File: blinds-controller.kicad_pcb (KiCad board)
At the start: 2 copper layers, 50.8 x 69.9 mm, 15 parts, among them J1 Jack-DC, J2 Conn_01x05_Female, U1 MP1584EN-LF-Z, U2 ESP32-S2-WROOM, U3 ULN2003A

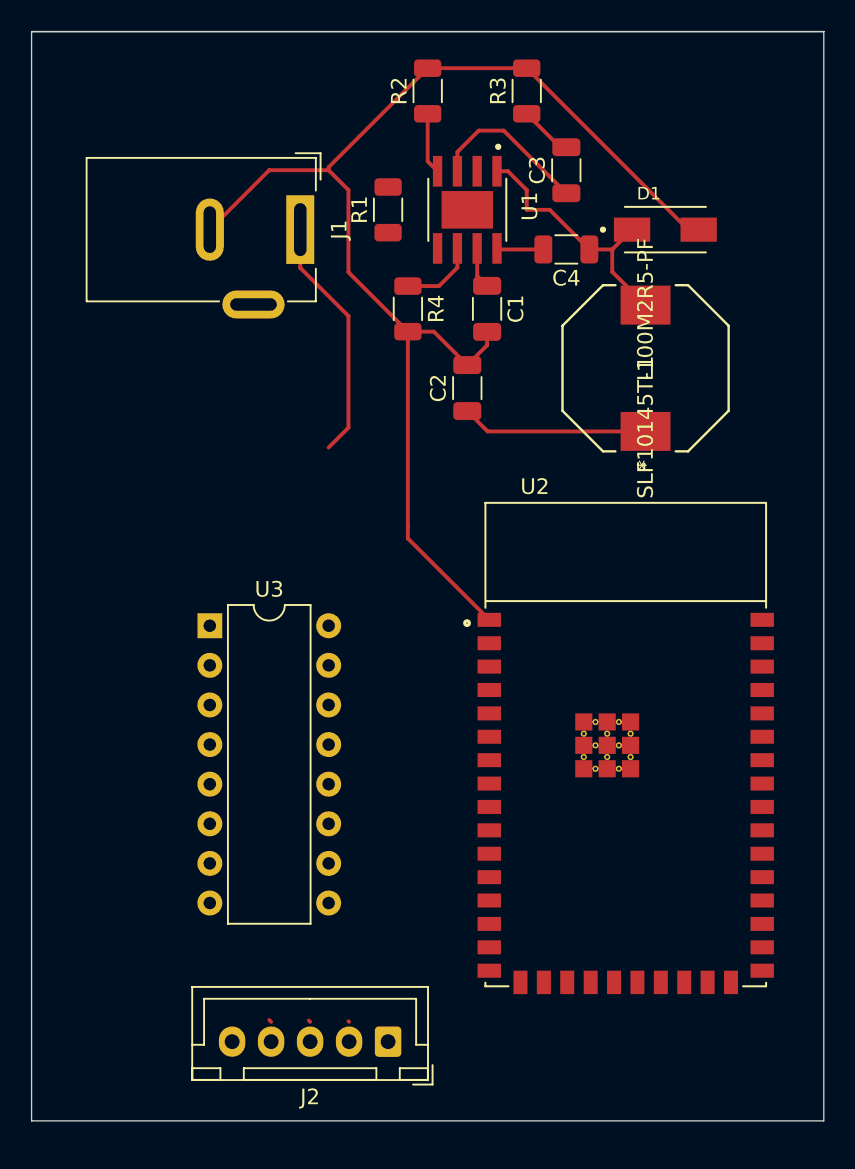
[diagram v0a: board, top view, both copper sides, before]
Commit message: First routed version of PCB
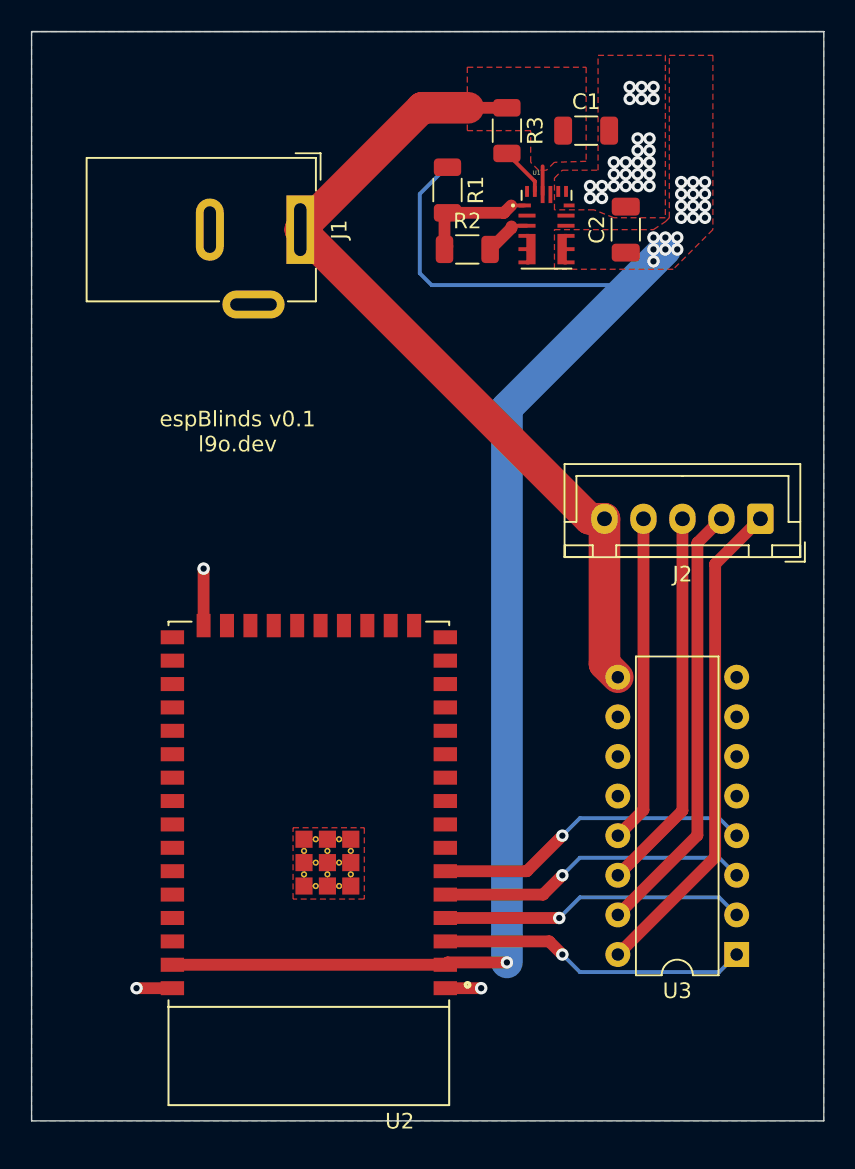
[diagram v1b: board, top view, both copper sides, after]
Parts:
- removed C3: 220pF, Capacitor_SMD:C_1206_3216Metric
- removed C4: 100nF, Capacitor_SMD:C_1206_3216Metric
- removed D1: B340A-13-F, B340A-13-F:DIOM5226X240N
- removed L1: SLF10145T-100M2R5-PF, SLF10145T-100:SLF10145T-100M2R5-PF
- removed R4: 200k, Resistor_SMD:R_1206_3216Metric
- C1: value 10uF -> 10uf
- R1: value 124k -> 75k
- R2: value 40.2k -> 24k
- R3: value 68.1k -> 100k
- U1: value MP1584EN-LF-Z -> MPM3610AGQV-P; footprint MP1584EN-LF-Z:SOIC127P600X170-9N -> footprints:CONV_MPM3620AGQV-P
- moved J2 41.2 mm to (100.1, 50.3)
- moved U3 39.8 mm to (98.6, 78.2), turned to 180 degrees
- moved U2 21.7 mm to (71.1, 72.4), turned to 180 degrees
- moved C2 14.4 mm to (91.4, 31.8)
- moved C1 13.1 mm to (88.9, 25.4), turned to 0 degrees
- moved R2 10.5 mm to (81.3, 33.0), turned to 0 degrees
- moved U1 5.24 mm to (86.4, 31.8), turned to 0 degrees
- moved R1 4.02 mm to (80.0, 29.2), turned to 270 degrees
- moved R3 2.84 mm to (83.8, 25.4), turned to 270 degrees
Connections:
- R3 pad 1: Net-(C3-Pad2) -> +12V
- R3 pad 2: GND -> Net-(R3-Pad2)
- U1 pad 1: Net-(C4-Pad1) -> Net-(R1-Pad2)
- U1 pad 3: Net-(C3-Pad1) -> GND
- U1 pad 4: Net-(R1-Pad2) -> Net-(U1-Pad19)
- U1 pad 5: GND -> Net-(U1-Pad19)
- U1 pad 6: Net-(R4-Pad1) -> Net-(U1-Pad19)
- U1 pad 7: +12V -> +3V3
- U1 pad 8: Net-(C4-Pad2) -> +3V3
- U1 pad 9: (no net) -> +3V3
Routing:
- net +3V3: track 12.0 -> 95.4 mm, vias 0 -> 20
- net GND: track 80.5 -> 11.3 mm, vias 0 -> 29
- net +12V: track 18.6 -> 56.0 mm
- net Net-(J2-Pad1): track 0.00 -> 31.7 mm
- net Net-(J2-Pad2): track 0.06 -> 28.2 mm
- net Net-(J2-Pad3): track 0.00 -> 24.6 mm
- net Net-(J2-Pad4): track 0.17 -> 21.0 mm
- net Stepper.D: track 0.00 -> 20.6 mm, vias 0 -> 1
- net Stepper.C: track 0.00 -> 20.1 mm, vias 0 -> 1
- net Stepper.A: track 0.00 -> 20.0 mm, vias 0 -> 1
- net Stepper.B: track 0.00 -> 19.7 mm, vias 0 -> 1
- net Net-(C4-Pad1): track 16.5 -> 0.00 mm
- net Net-(C3-Pad1): track 10.5 -> 0.00 mm
- net Net-(R4-Pad1): track 4.90 -> 0.00 mm
- net Net-(R1-Pad2): track 3.95 -> 8.23 mm
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- added copper zone on F.Cu, net +12V
- added copper zone on F.Cu, net +3V3
- added copper zone on B.Cu, net GND
- added copper zone on F.Cu, net GND
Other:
- board text added: "espBlinds v0.1 l9o.dev"

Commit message: Added headers for testing voltage
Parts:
- added J3: DC Check, Connector_PinHeader_2.54mm:PinHeader_1x03_P2.54mm_Vertical, F.Cu at (75.2, 42.7)
- J2: value Conn_01x05_Female -> Stepper Motor
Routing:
- net +3V3: track 95.4 -> 104.1 mm
- net +12V: track 56.0 -> 60.5 mm
- net GND: vias 29 -> 30

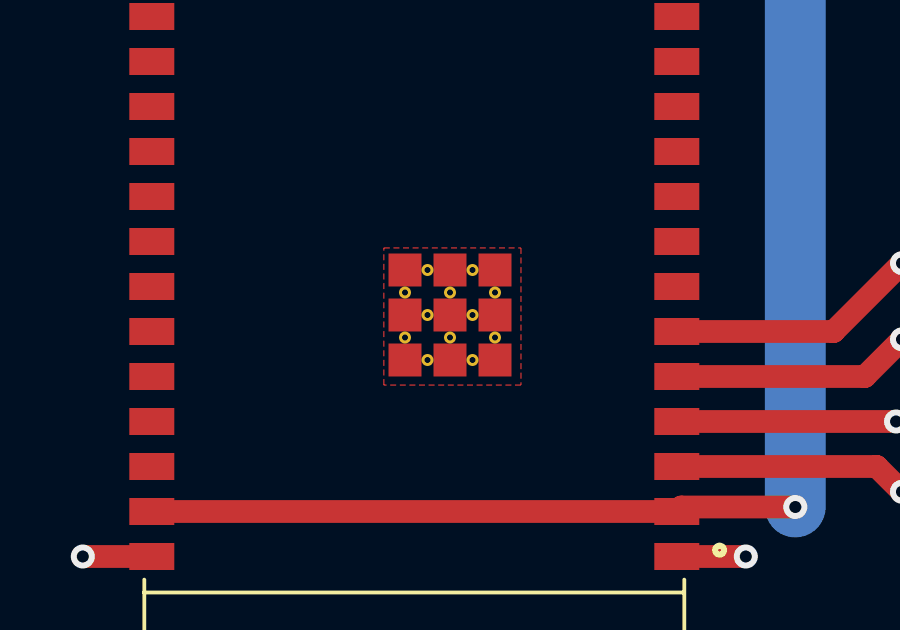
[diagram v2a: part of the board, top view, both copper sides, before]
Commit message: Added traces between GND pins on ESP32 bottom
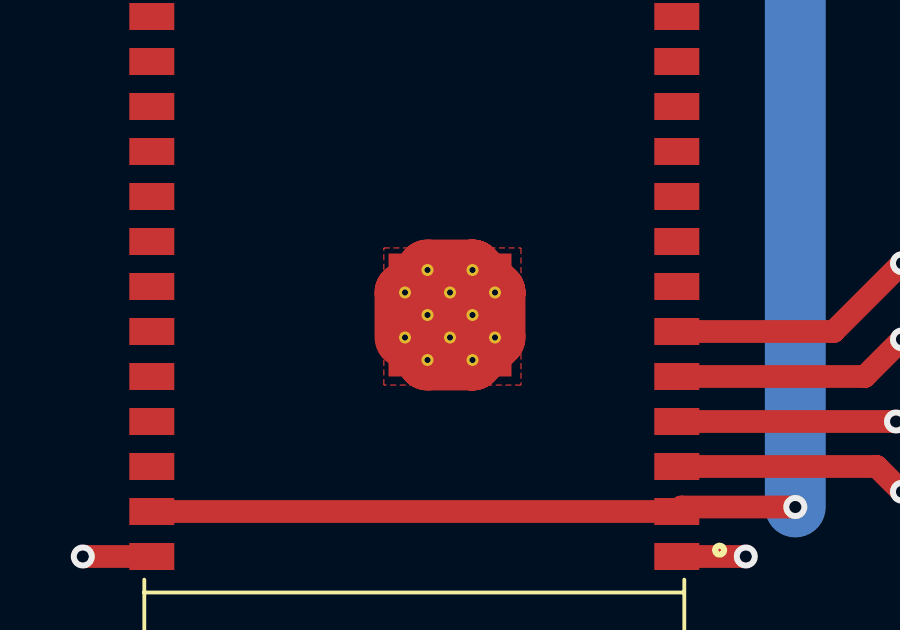
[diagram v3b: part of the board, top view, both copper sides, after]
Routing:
- net GND: track 11.3 -> 30.1 mm
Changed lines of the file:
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@@
     (thickness 1.6)
     (drawings 6)
-    (tracks 131)
+    (tracks 147)
     (zones 0)
     (modules 11)
@@
   (segment (start 83.78925 31.97325) (end 84.11383 31.64867) (width 0.76) (layer F.Cu) (net 2))
   (via (at 83.78925 31.97325) (size 0.8) (drill 0.4) (layers F.Cu B.Cu) (net 2))
+  (segment (start 73.06 70.84) (end 71.56 70.84) (width 2.03) (layer F.Cu) (net 2))
+  (segment (start 70.81 71.59) (end 70.81 73.09) (width 2.03) (layer F.Cu) (net 2))
+  (segment (start 71.56 73.84) (end 73.06 73.84) (width 2.03) (layer F.Cu) (net 2))
+  (segment (start 73.06 73.84) (end 73.81 73.09) (width 2.03) (layer F.Cu) (net 2))
+  (segment (start 73.81 73.09) (end 73.81 71.59) (width 2.03) (layer F.Cu) (net 2))
+  (segment (start 73.81 71.59) (end 73.06 70.84) (width 2.03) (layer F.Cu) (net 2))
+  (segment (start 72.31 73.09) (end 71.56 72.34) (width 2.03) (layer F.Cu) (net 2))
+  (segment (start 71.56 72.34) (end 72.31 71.59) (width 2.03) (layer F.Cu) (net 2))
+  (segment (start 72.31 71.59) (end 73.06 72.34) (width 2.03) (layer F.Cu) (net 2))
+  (segment (start 73.06 72.34) (end 72.31 73.09) (width 2.03) (layer F.Cu) (net 2))
+  (segment (start 71.56 72.34) (end 70.81 71.59) (width 2.03) (layer F.Cu) (net 2))
+  (segment (start 72.31 73.09) (end 71.56 73.84) (width 2.03) (layer F.Cu) (net 2))
+  (segment (start 72.31 73.09) (end 73.06 73.84) (width 2.03) (layer F.Cu) (net 2))
+  (segment (start 73.06 72.34) (end 73.81 71.59) (width 2.03) (layer F.Cu) (net 2))
+  (segment (start 72.31 71.59) (end 73.06 70.84) (width 2.03) (layer F.Cu) (net 2))
+  (segment (start 72.31 71.59) (end 71.56 70.84) (width 2.03) (layer F.Cu) (net 2))
   (segment (start 92.576 68.968) (end 90.932 70.612) (width 0.76) (layer F.Cu) (net 3))
   (segment (start 92.576 50.292) (end 92.576 68.968) (width 0.76) (layer F.Cu) (net 3))

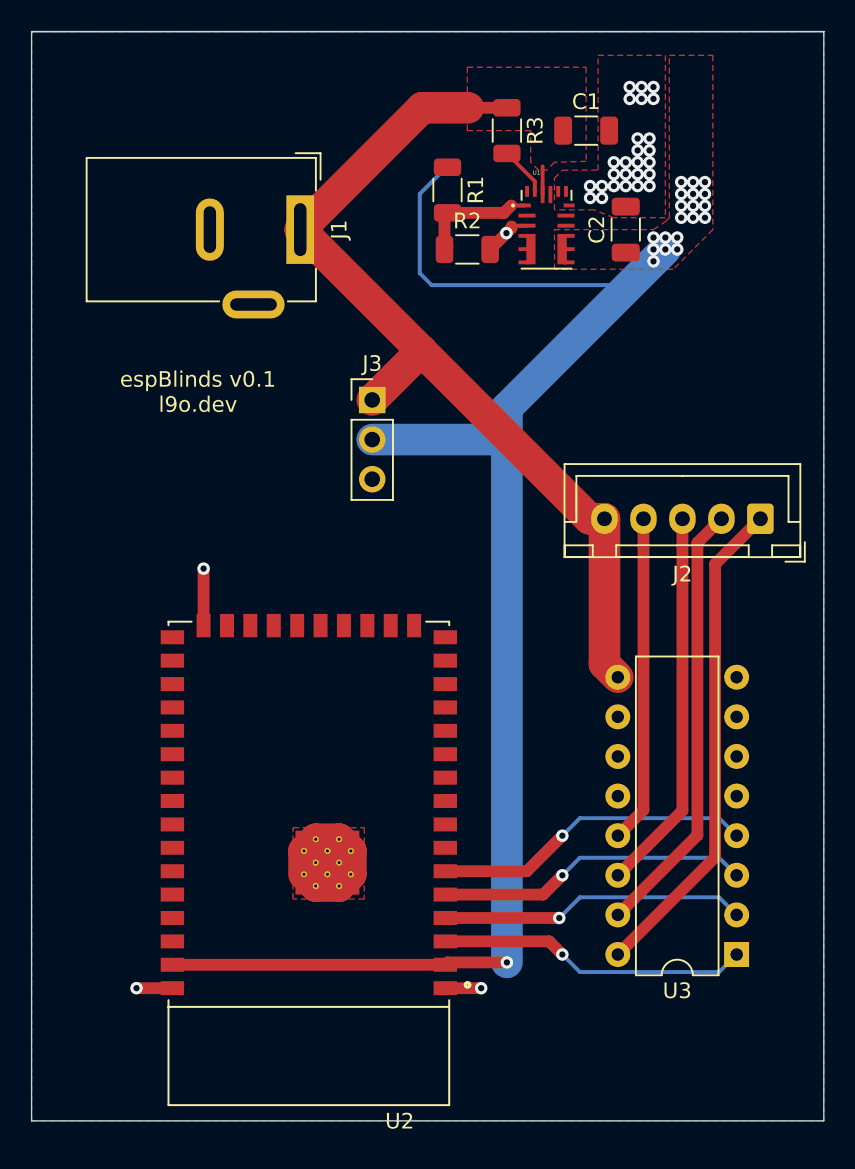
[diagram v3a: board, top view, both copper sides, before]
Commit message: Added JTAG connector
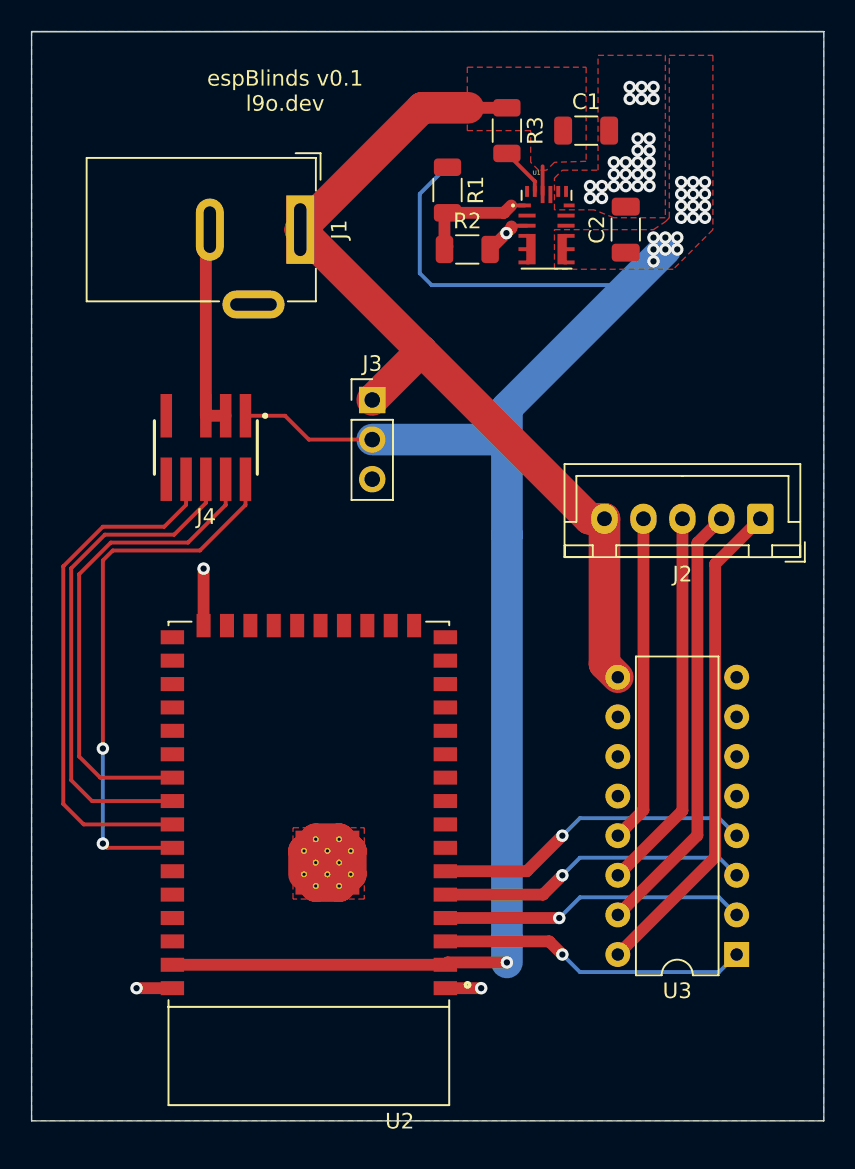
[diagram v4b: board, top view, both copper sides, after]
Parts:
- added J4: JTAG, footprints:SAMTEC_FTSH-105-01-L-DV-007-K-P-TR, F.Cu at (64.5, 45.7)
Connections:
- U2 pad 33: (no net) -> JTAG.TCK
- U2 pad 34: (no net) -> JTAG.TDO
- U2 pad 35: (no net) -> JTAG.TDI
- U2 pad 36: (no net) -> JTAG.TMS
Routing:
- net JTAG.TMS: track 0.00 -> 35.0 mm, vias 0 -> 2
- net JTAG.TDI: track 0.00 -> 33.9 mm
- net JTAG.TDO: track 0.00 -> 32.5 mm
- net JTAG.TCK: track 0.00 -> 31.1 mm
- net GND: track 30.1 -> 43.6 mm
- net +3V3: track 104.1 -> 113.5 mm

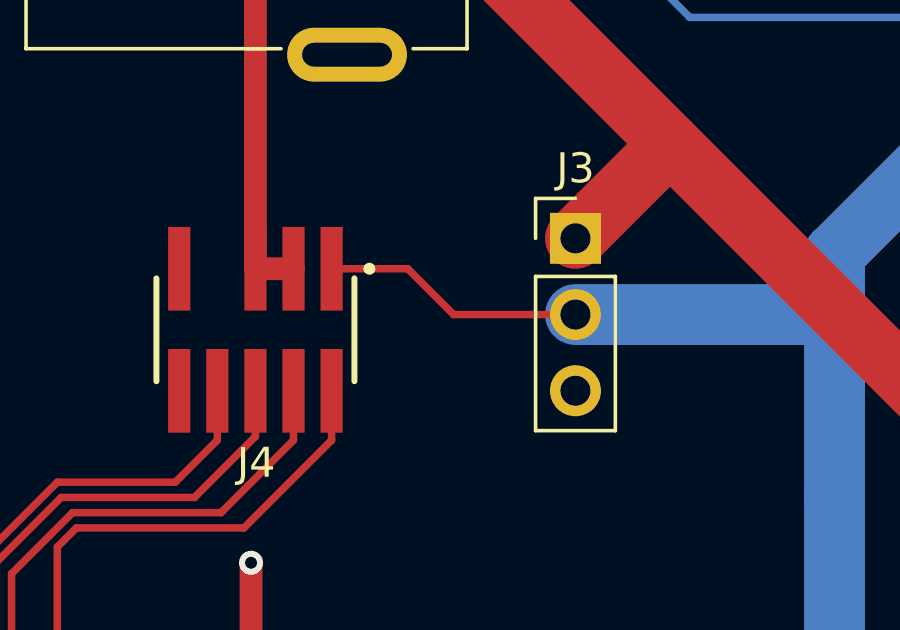
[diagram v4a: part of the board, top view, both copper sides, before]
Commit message: Added labels to DC check header
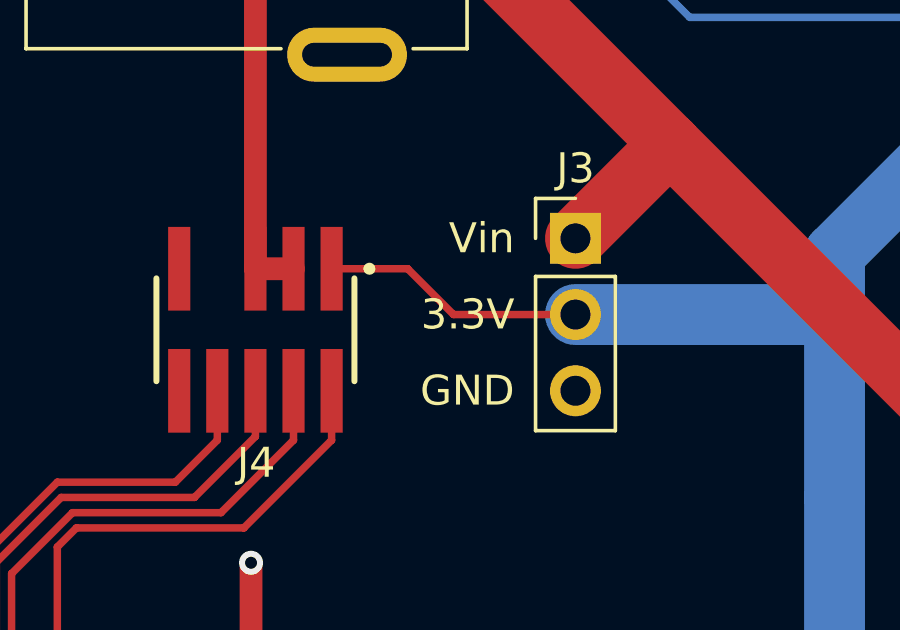
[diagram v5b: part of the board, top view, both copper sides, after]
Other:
- board text added: "3.3V"
- board text added: "GND"
- board text added: "Vin"
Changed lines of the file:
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@@
   (general
     (thickness 1.6)
-    (drawings 6)
+    (drawings 9)
     (tracks 189)
     (zones 0)
@@
       (net 2 GND))
   )
+  (gr_text "GND\n" (at 73.152 47.752) (layer F.SilkS)
+    (effects (font (size 1 1) (thickness 0.15)) (justify right))
+  )
+  (gr_text "3.3V\n" (at 73.152 45.212) (layer F.SilkS)
+    (effects (font (size 1 1) (thickness 0.15)) (justify right))
+  )
+  (gr_text "Vin\n" (at 73.152 42.672) (layer F.SilkS)
+    (effects (font (size 1 1) (thickness 0.15)) (justify right))
+  )
   (gr_text "espBlinds v0.1\nl9o.dev" (at 69.596 22.86) (layer F.SilkS)

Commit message: Lots of small tweaks, almost there
Just missing decoupling capacitors and a final review
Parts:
- added REF**: MountingHole_2.2mm_M2_DIN965_Pad, MountingHole:MountingHole_2.2mm_M2_DIN965_Pad, F.Cu at (101.6, 20.8)
- added REF**: MountingHole_2.2mm_M2_DIN965_Pad, MountingHole:MountingHole_2.2mm_M2_DIN965_Pad, F.Cu at (101.6, 87.3)
- added REF**: MountingHole_2.2mm_M2_DIN965_Pad, MountingHole:MountingHole_2.2mm_M2_DIN965_Pad, F.Cu at (55.1, 87.3)
- added REF**: MountingHole_2.2mm_M2_DIN965_Pad, MountingHole:MountingHole_2.2mm_M2_DIN965_Pad, F.Cu at (55.1, 20.8)
- J1: value Jack-DC -> DC Jack
- J3: value DC Check -> Power
- moved J1 4.13 mm to (67.5, 29.0)
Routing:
- net GND: track 43.6 -> 31.5 mm, vias 30 -> 31
- net +12V: track 60.5 -> 66.6 mm
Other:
- board size 50.8 x 69.9 mm -> 50 x 70 mm
